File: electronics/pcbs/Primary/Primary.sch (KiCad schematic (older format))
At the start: 26 parts, among them J1 Line Sensor 1, J11 I2C Bus, J12 Battery, J13 Pololu_D24V50F5, J14 Magnet, J2 Line Sensor 2, J3 Line Sensor 3, J4 Line Sensor 4, J5 Line Sensor 5, J6 Line Sensor 6, J7 Servo, J8 Pololu_DRV8834, J9 Stepper Motor, P1 Digital, P10 CONN_01X01, P11 CONN_01X01, P12 CONN_01X01, P13 CONN_01X01, P2 Power, P3 Analog, P4 Analog, P5 PWM, P6 PWM, P7 Communication, P8 CONN_01X01, P9 CONN_01X01

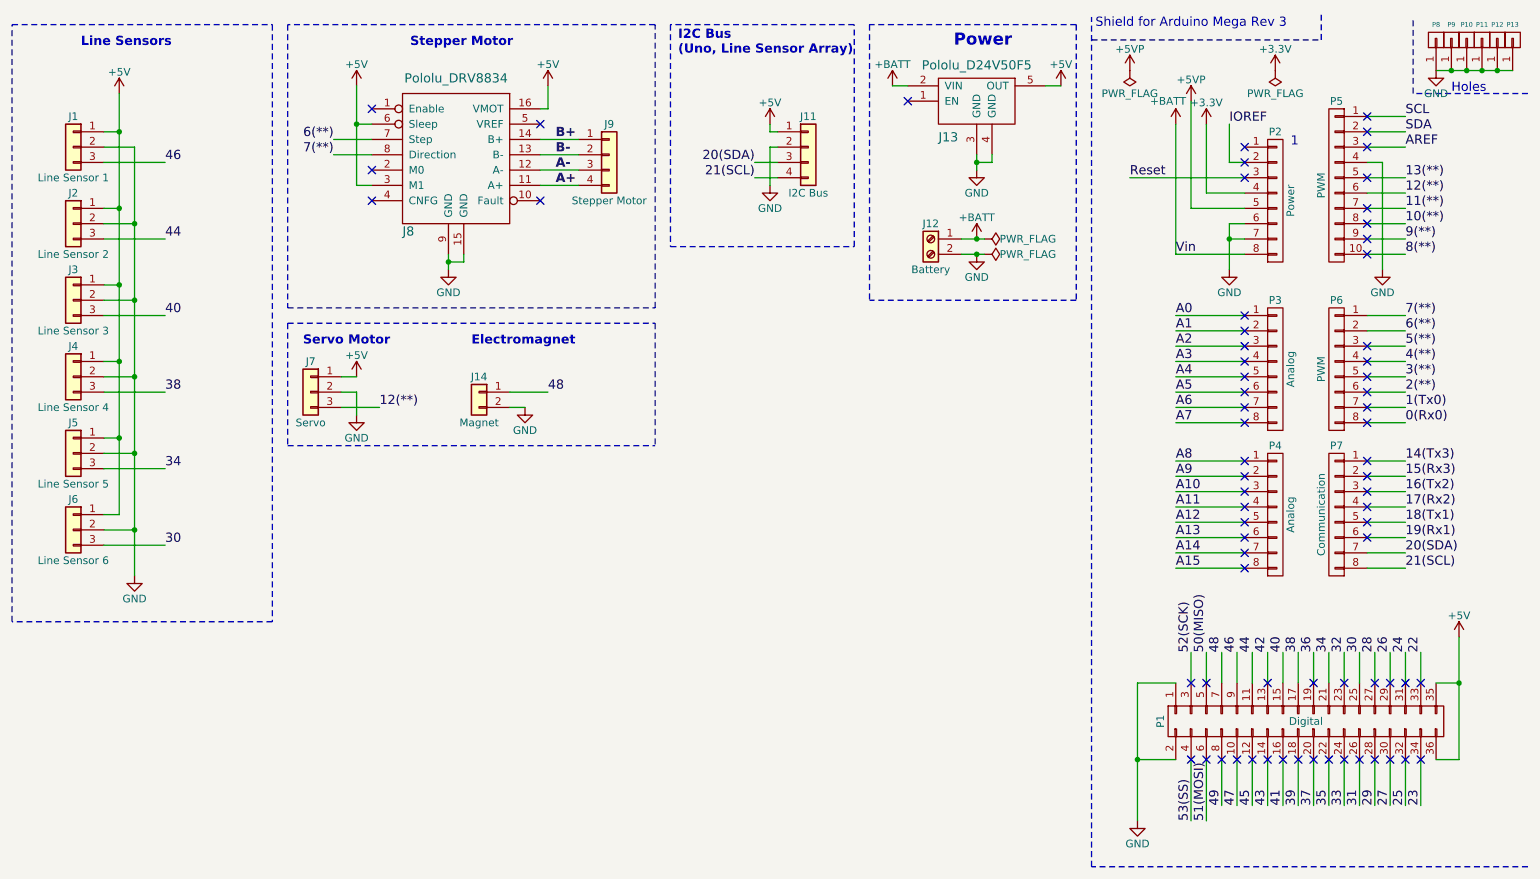
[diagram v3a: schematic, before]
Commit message: Primary PCB: Modified electromagnet circuit to power the magnet with a transistor.
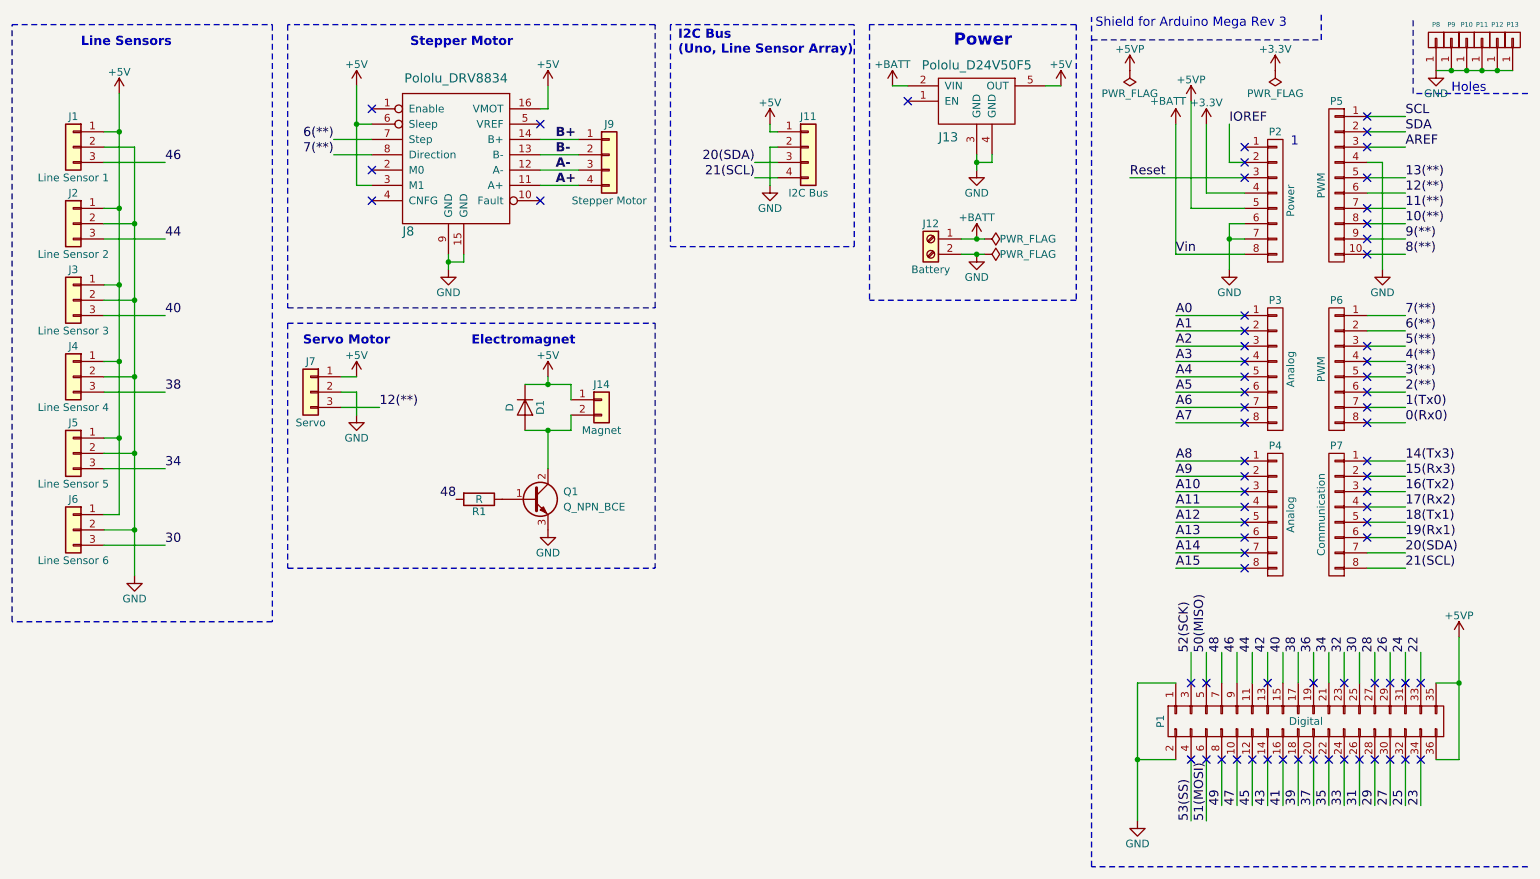
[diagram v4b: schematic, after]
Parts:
- added D1: D, Diodes_THT:D_DO-15_P5.08mm_Vertical_KathodeUp, symbol D
- added Q1: Q_NPN_BCE, TO_SOT_Packages_THT:TO-92_Inline_Wide, symbol Q_NPN_BCE
- added R1: R, Resistors_THT:R_Axial_DIN0309_L9.0mm_D3.2mm_P5.08mm_Vertical, symbol R
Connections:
- net +5V: now also J14.1 (Pin_1), D1.1 (K); no longer P1.35 (P35), P1.36 (P36)
- net +5VP: now also P1.35 (P35), P1.36 (P36)
- net 48: now also R1.2; no longer J14.1 (Pin_1)
- net GND: now also Q1.3 (E); no longer J14.2 (Pin_2)
- new net: D1.2 (A), J14.2 (Pin_2), Q1.2 (C)
- new net: Q1.1 (B), R1.1
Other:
- moved on the sheet: J14
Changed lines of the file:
@@
 Title "Primary Region V Bot"
 Date "2018-03-21"
-Rev "2"
+Rev "3"
 Comp "IEEE RAS (UT)"
-Comment1 "Rev 2: The Mega is now powered by +BATT"
-Comment2 ""
+Comment1 "Rev 3: The magnet is driven by a transistor now."
+Comment2 "Rev 2: The Mega is now powered by +BATT"
 Comment3 ""
 Comment4 ""
@@
 $EndComp
 $Comp
-L +5V #PWR05
-U 1 1 56D75AB8
-P 10750 4550
-F 0 "#PWR05" H 10750 4400 50  0001 C CNN
-F 1 "+5V" H 10750 4690 50  0000 C CNN
-F 2 "" H 10750 4550 50  0000 C CNN
-F 3 "" H 10750 4550 50  0000 C CNN
-	1    10750 4550
-	1    0    0    -1
-$EndComp
-$Comp
 L Conn_01x03 J3
 U 1 1 5AB06CE7
@@
 $EndComp
 $Comp
-L GND #PWR06
+L GND #PWR05
 U 1 1 5AB07E69
 P 2100 4150
-F 0 "#PWR06" H 2100 3900 50  0001 C CNN
+F 0 "#PWR05" H 2100 3900 50  0001 C CNN
 F 1 "GND" H 2100 4000 50  0000 C CNN
 F 2 "" H 2100 4150 50  0000 C CNN
@@
 NoConn ~ 3650 1700
 $Comp
-L GND #PWR07
+L GND #PWR06
 U 1 1 5AB0A94E
 P 4150 2150
-F 0 "#PWR07" H 4150 1900 50  0001 C CNN
+F 0 "#PWR06" H 4150 1900 50  0001 C CNN
 F 1 "GND" H 4150 2000 50  0000 C CNN
 F 2 "" H 4150 2150 50  0000 C CNN
@@
 Stepper Motor
 $Comp
-L +5V #PWR08
+L +5V #PWR07
 U 1 1 5AB0B79A
 P 2000 1000
-F 0 "#PWR08" H 2000 850 50  0001 C CNN
+F 0 "#PWR07" H 2000 850 50  0001 C CNN
 F 1 "+5V" H 2000 1140 50  0000 C CNN
 F 2 "" H 2000 1000 50  0000 C CNN
@@
 $EndComp
 $Comp
-L +5V #PWR09
+L +5V #PWR08
 U 1 1 5AB0BB75
 P 3550 950
-F 0 "#PWR09" H 3550 800 50  0001 C CNN
+F 0 "#PWR08" H 3550 800 50  0001 C CNN
 F 1 "+5V" H 3550 1090 50  0000 C CNN
 F 2 "" H 3550 950 50  0000 C CNN
@@
 $EndComp
 $Comp
-L +5V #PWR010
+L +5V #PWR09
 U 1 1 5AB0BCF7
 P 4800 950
-F 0 "#PWR010" H 4800 800 50  0001 C CNN
+F 0 "#PWR09" H 4800 800 50  0001 C CNN
 F 1 "+5V" H 4800 1090 50  0000 C CNN
 F 2 "" H 4800 950 50  0000 C CNN
@@
 $EndComp
 $Comp
-L +5V #PWR011
-U 1 1 5AB0C699
-P 6250 1200
-F 0 "#PWR011" H 6250 1050 50  0001 C CNN
-F 1 "+5V" H 6250 1340 50  0000 C CNN
-F 2 "" H 6250 1200 50  0000 C CNN
-F 3 "" H 6250 1200 50  0000 C CNN
-	1    6250 1200
-	1    0    0    -1
-$EndComp
-$Comp
-L GND #PWR012
+L GND #PWR010
 U 1 1 5AB0CA84
 P 6250 1600
-F 0 "#PWR012" H 6250 1350 50  0001 C CNN
+F 0 "#PWR010" H 6250 1350 50  0001 C CNN
 F 1 "GND" H 6250 1450 50  0000 C CNN
 F 2 "" H 6250 1600 50  0000 C CNN
@@
 Servo Motor
 $Comp
-L +5V #PWR013
+L +5V #PWR011
 U 1 1 5AB127F7
 P 3550 2850
-F 0 "#PWR013" H 3550 2700 50  0001 C CNN
+F 0 "#PWR011" H 3550 2700 50  0001 C CNN
 F 1 "+5V" H 3550 2990 50  0000 C CNN
 F 2 "" H 3550 2850 50  0000 C CNN
@@
 $EndComp
 $Comp
-L GND #PWR014
+L GND #PWR012
 U 1 1 5AB1284A
 P 3550 3100
-F 0 "#PWR014" H 3550 2850 50  0001 C CNN
+F 0 "#PWR012" H 3550 2850 50  0001 C CNN
 F 1 "GND" H 3550 2950 50  0000 C CNN
 F 2 "" H 3550 3100 50  0000 C CNN
@@
 	3550 2850 3450 2850
 Wire Notes Line
-	3100 2500 3100 3300
-Wire Notes Line
-	3100 3300 5500 3300
+	3100 2500 3100 4100
+Wire Notes Line
+	3100 4100 5500 4100
 Wire Notes Line
 	3100 2500 5500 2500
@@
 NoConn ~ 7150 1050
 $Comp
-L GND #PWR015
+L GND #PWR013
 U 1 1 5AB13861
 P 7600 1500
-F 0 "#PWR015" H 7600 1250 50  0001 C CNN
+F 0 "#PWR013" H 7600 1250 50  0001 C CNN
 F 1 "GND" H 7600 1350 50  0000 C CNN
 F 2 "" H 7600 1500 50  0000 C CNN
@@
 Connection ~ 7600 1450
 $Comp
-L +BATT #PWR016
+L +BATT #PWR014
 U 1 1 5AB13B80
 P 7050 950
-F 0 "#PWR016" H 7050 800 50  0001 C CNN
+F 0 "#PWR014" H 7050 800 50  0001 C CNN
 F 1 "+BATT" H 7050 1090 50  0000 C CNN
 F 2 "" H 7050 950 50  0001 C CNN
@@
 $EndComp
 $Comp
-L +BATT #PWR017
+L +BATT #PWR015
 U 1 1 5AB16019
 P 7600 1950
-F 0 "#PWR017" H 7600 1800 50  0001 C CNN
+F 0 "#PWR015" H 7600 1800 50  0001 C CNN
 F 1 "+BATT" H 7600 2090 50  0000 C CNN
 F 2 "" H 7600 1950 50  0001 C CNN
@@
 $EndComp
 $Comp
-L GND #PWR018
+L GND #PWR016
 U 1 1 5AB16072
 P 7600 2050
-F 0 "#PWR018" H 7600 1800 50  0001 C CNN
+F 0 "#PWR016" H 7600 1800 50  0001 C CNN
 F 1 "GND" H 7600 1900 50  0000 C CNN
 F 2 "" H 7600 2050 50  0000 C CNN
@@
 $EndComp
 $Comp
-L PWR_FLAG #FLG019
+L PWR_FLAG #FLG017
 U 1 1 5AB160ED
 P 7650 1950
-F 0 "#FLG019" H 7650 2025 50  0001 C CNN
+F 0 "#FLG017" H 7650 2025 50  0001 C CNN
 F 1 "PWR_FLAG" V 7650 2050 50  0000 L CNN
 F 2 "" H 7650 1950 50  0001 C CNN
@@
 $EndComp
 $Comp
-L PWR_FLAG #FLG020
+L PWR_FLAG #FLG018
 U 1 1 5AB1614D
 P 7650 2050
-F 0 "#FLG020" H 7650 2125 50  0001 C CNN
+F 0 "#FLG018" H 7650 2125 50  0001 C CNN
 F 1 "PWR_FLAG" V 7650 2150 50  0000 L CNN
 F 2 "" H 7650 2050 50  0001 C CNN
@@
 Connection ~ 7600 2050
 $Comp
-L PWR_FLAG #FLG021
+L PWR_FLAG #FLG019
 U 1 1 5AB1CAC7
 P 8600 850
-F 0 "#FLG021" H 8600 925 50  0001 C CNN
+F 0 "#FLG019" H 8600 925 50  0001 C CNN
 F 1 "PWR_FLAG" H 8600 1000 50  0000 C CNN
 F 2 "" H 8600 850 50  0001 C CNN
@@
 $EndComp
 $Comp
-L PWR_FLAG #FLG022
+L PWR_FLAG #FLG020
 U 1 1 5AB1CCDE
 P 9550 850
-F 0 "#FLG022" H 9550 925 50  0001 C CNN
+F 0 "#FLG020" H 9550 925 50  0001 C CNN
 F 1 "PWR_FLAG" H 9550 1000 50  0000 C CNN
 F 2 "" H 9550 850 50  0001 C CNN
@@
 $EndComp
 $Comp
-L +3.3V #PWR023
+L +3.3V #PWR021
 U 1 1 5AB1CD37
 P 9550 850
-F 0 "#PWR023" H 9550 700 50  0001 C CNN
+F 0 "#PWR021" H 9550 700 50  0001 C CNN
 F 1 "+3.3V" H 9550 990 50  0000 C CNN
 F 2 "" H 9550 850 50  0000 C CNN
@@
 L Conn_01x02 J14
 U 1 1 5AB1EC74
-P 4350 2950
-F 0 "J14" H 4350 3050 50  0000 C CNN
-F 1 "Magnet" H 4350 2750 50  0000 C CNN
-F 2 "Connectors_Samtec:SL-102-X-XX_1x02" H 4350 2950 50  0001 C CNN
-F 3 "" H 4350 2950 50  0001 C CNN
-	1    4350 2950
-	-1   0    0    -1
-$EndComp
-$Comp
-L GND #PWR024
+P 5150 3000
+F 0 "J14" H 5150 3100 50  0000 C CNN
+F 1 "Magnet" H 5150 2800 50  0000 C CNN
+F 2 "Connectors_Samtec:SL-102-X-XX_1x02" H 5150 3000 50  0001 C CNN
+F 3 "" H 5150 3000 50  0001 C CNN
+	1    5150 3000
+	1    0    0    -1
+$EndComp
+$Comp
+L GND #PWR022
 U 1 1 5AB1ECFA
-P 4650 3050
-F 0 "#PWR024" H 4650 2800 50  0001 C CNN
-F 1 "GND" H 4650 2900 50  0000 C CNN
-F 2 "" H 4650 3050 50  0000 C CNN
-F 3 "" H 4650 3050 50  0000 C CNN
-	1    4650 3050
-	1    0    0    -1
-$EndComp
-Wire Wire Line
-	4550 3050 4650 3050
+P 4800 3850
+F 0 "#PWR022" H 4800 3600 50  0001 C CNN
+F 1 "GND" H 4800 3700 50  0000 C CNN
+F 2 "" H 4800 3850 50  0000 C CNN
+F 3 "" H 4800 3850 50  0000 C CNN
+	1    4800 3850
+	1    0    0    -1
+$EndComp
 Text Notes 4300 2650 0    60   ~ 12
 Electromagnet
-Wire Wire Line
-	4550 2950 4800 2950
-Wire Notes Line
-	5500 2500 5500 3300
+Wire Notes Line
+	5500 2500 5500 4100
 Text Label 4850 1300 0    60   ~ 12
 B+
@@
 Text Label 3700 3050 0    60   ~ 0
 12(**)
-Text Label 4800 2950 0    60   ~ 0
+Text Label 4200 3650 2    60   ~ 0
 48
 Text Label 2300 1450 0    60   ~ 0
@@
 NoConn ~ 9500 4850
 $Comp
-L +5VP #PWR025
+L +5VP #PWR023
 U 1 1 5AB27247
 P 9000 1050
-F 0 "#PWR025" H 9000 900 50  0001 C CNN
+F 0 "#PWR023" H 9000 900 50  0001 C CNN
 F 1 "+5VP" H 9000 1190 50  0000 C CNN
 F 2 "" H 9000 1050 50  0001 C CNN
@@
 $EndComp
 $Comp
-L +5V #PWR026
+L +5V #PWR024
 U 1 1 5AB272C7
 P 8150 950
-F 0 "#PWR026" H 8150 800 50  0001 C CNN
+F 0 "#PWR024" H 8150 800 50  0001 C CNN
 F 1 "+5V" H 8150 1090 50  0000 C CNN
 F 2 "" H 8150 950 50  0000 C CNN
@@
 	8050 950  8150 950
 $Comp
-L +5VP #PWR027
+L +5VP #PWR025
 U 1 1 5AB2840B
 P 8600 850
-F 0 "#PWR027" H 8600 700 50  0001 C CNN
+F 0 "#PWR025" H 8600 700 50  0001 C CNN
 F 1 "+5VP" H 8600 990 50  0000 C CNN
 F 2 "" H 8600 850 50  0001 C CNN
@@
 $EndComp
 $Comp
-L GND #PWR028
+L GND #PWR026
 U 1 1 5AB165B1
 P 10600 850
-F 0 "#PWR028" H 10600 600 50  0001 C CNN
+F 0 "#PWR026" H 10600 600 50  0001 C CNN
 F 1 "GND" H 10600 700 50  0000 C CNN
 F 2 "" H 10600 850 50  0000 C CNN
@@
 Connection ~ 11000 850
 $Comp
-L +BATT #PWR029
+L +BATT #PWR027
 U 1 1 5AB2CF23
 P 8900 1200
-F 0 "#PWR029" H 8900 1050 50  0001 C CNN
+F 0 "#PWR027" H 8900 1050 50  0001 C CNN
 F 1 "+BATT" H 8850 1350 50  0000 C CNN
 F 2 "" H 8900 1200 50  0001 C CNN
@@
 Wire Wire Line
 	6300 1550 6150 1550
+$Comp
+L R R1
+U 1 1 5AC00307
+P 4350 3650
+F 0 "R1" V 4430 3650 50  0000 C CNN
+F 1 "R" V 4350 3650 50  0000 C CNN
+F 2 "Resistors_THT:R_Axial_DIN0309_L9.0mm_D3.2mm_P5.08mm_Vertical" V 4280 3650 50  0001 C CNN
+F 3 "" H 4350 3650 50  0001 C CNN
+	1    4350 3650
+	0    1    1    0
+$EndComp
+$Comp
+L Q_NPN_BCE Q1
+U 1 1 5AC00358
+P 4700 3650
+F 0 "Q1" H 4900 3700 50  0000 L CNN
+F 1 "Q_NPN_BCE" H 4900 3600 50  0000 L CNN
+F 2 "TO_SOT_Packages_THT:TO-92_Inline_Wide" H 4900 3750 50  0001 C CNN
+F 3 "" H 4700 3650 50  0001 C CNN
+	1    4700 3650
+	1    0    0    -1
+$EndComp
+$Comp
+L +5V #PWR028
+U 1 1 5AC005CD
+P 4800 2850
+F 0 "#PWR028" H 4800 2700 50  0001 C CNN
+F 1 "+5V" H 4800 2990 50  0000 C CNN
+F 2 "" H 4800 2850 50  0000 C CNN
+F 3 "" H 4800 2850 50  0000 C CNN
+	1    4800 2850
+	1    0    0    -1
+$EndComp
+$Comp
+L +5V #PWR029
+U 1 1 5AC026E1
+P 6250 1200
+F 0 "#PWR029" H 6250 1050 50  0001 C CNN
+F 1 "+5V" H 6250 1340 50  0000 C CNN
+F 2 "" H 6250 1200 50  0000 C CNN
+F 3 "" H 6250 1200 50  0000 C CNN
+	1    6250 1200
+	1    0    0    -1
+$EndComp
+$Comp
+L D D1
+U 1 1 5AC02CCD
+P 4650 3050
+F 0 "D1" H 4650 3150 50  0000 C CNN
+F 1 "D" H 4650 2950 50  0000 C CNN
+F 2 "Diodes_THT:D_DO-15_P5.08mm_Vertical_KathodeUp" H 4650 3050 50  0001 C CNN
+F 3 "" H 4650 3050 50  0001 C CNN
+	1    4650 3050
+	0    1    1    0
+$EndComp
+Wire Wire Line
+	4950 2900 4950 3000
+Wire Wire Line
+	4650 2900 4950 2900
+Wire Wire Line
+	4800 2900 4800 2850
+Connection ~ 4800 2900
+Wire Wire Line
+	4650 3200 4950 3200
+Wire Wire Line
+	4800 3200 4800 3450
+Wire Wire Line
+	4950 3200 4950 3100
+Connection ~ 4800 3200
+$Comp
+L +5VP #PWR030
+U 1 1 5AC03CD4
+P 10750 4550
+F 0 "#PWR030" H 10750 4400 50  0001 C CNN
+F 1 "+5VP" H 10750 4690 50  0000 C CNN
+F 2 "" H 10750 4550 50  0001 C CNN
+F 3 "" H 10750 4550 50  0001 C CNN
+	1    10750 4550
+	1    0    0    -1
+$EndComp
 $EndSCHEMATC

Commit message: Primary PCB: Corrected transistor pinout and footprint. Gave a value to the resistor attached to the transistor.
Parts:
- D1: value D -> 1N914
- Q1: footprint TO_SOT_Packages_THT:TO-92_Inline_Wide -> TO_SOT_Packages_THT:TO-18-3; symbol Q_NPN_BCE -> Q_NPN_EBC
- R1: value R -> 220
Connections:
- net GND: now also Q1.1 (E); no longer Q1.3 (E)
- net at D1.2 (A), J14.2 (Pin_2): now also Q1.3 (C); no longer Q1.2 (C)
- net at R1.1: now also Q1.2 (B); no longer Q1.1 (B)
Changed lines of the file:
@@
 P 4350 3650
 F 0 "R1" V 4430 3650 50  0000 C CNN
-F 1 "R" V 4350 3650 50  0000 C CNN
+F 1 "220" V 4350 3650 50  0000 C CNN
 F 2 "Resistors_THT:R_Axial_DIN0309_L9.0mm_D3.2mm_P5.08mm_Vertical" V 4280 3650 50  0001 C CNN
 F 3 "" H 4350 3650 50  0001 C CNN
@@
 $EndComp
 $Comp
-L Q_NPN_BCE Q1
+L Q_NPN_EBC Q1
 U 1 1 5AC00358
 P 4700 3650
 F 0 "Q1" H 4900 3700 50  0000 L CNN
 F 1 "Q_NPN_BCE" H 4900 3600 50  0000 L CNN
-F 2 "TO_SOT_Packages_THT:TO-92_Inline_Wide" H 4900 3750 50  0001 C CNN
+F 2 "TO_SOT_Packages_THT:TO-18-3" H 4900 3750 50  0001 C CNN
 F 3 "" H 4700 3650 50  0001 C CNN
 	1    4700 3650
@@
 P 4650 3050
 F 0 "D1" H 4650 3150 50  0000 C CNN
-F 1 "D" H 4650 2950 50  0000 C CNN
+F 1 "1N914" H 4650 2950 50  0000 C CNN
 F 2 "Diodes_THT:D_DO-15_P5.08mm_Vertical_KathodeUp" H 4650 3050 50  0001 C CNN
 F 3 "" H 4650 3050 50  0001 C CNN

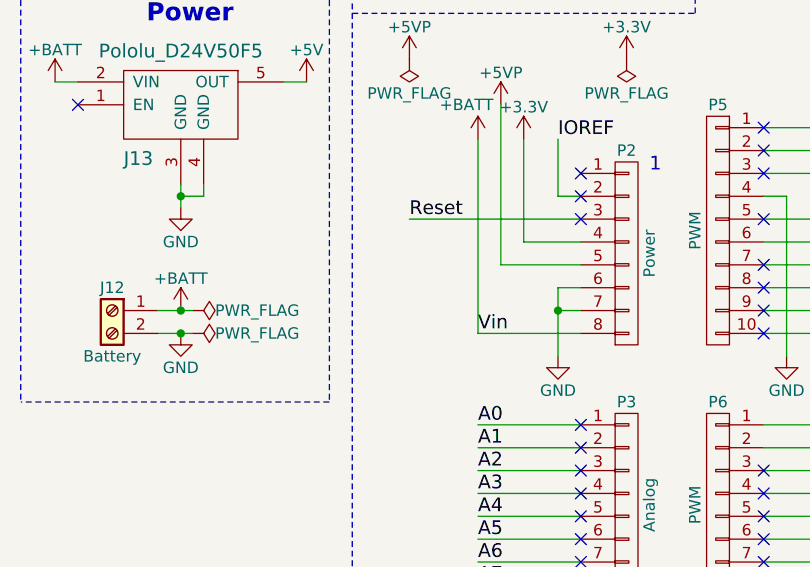
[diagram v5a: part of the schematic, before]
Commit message: Primary PCB: Added Reset button.
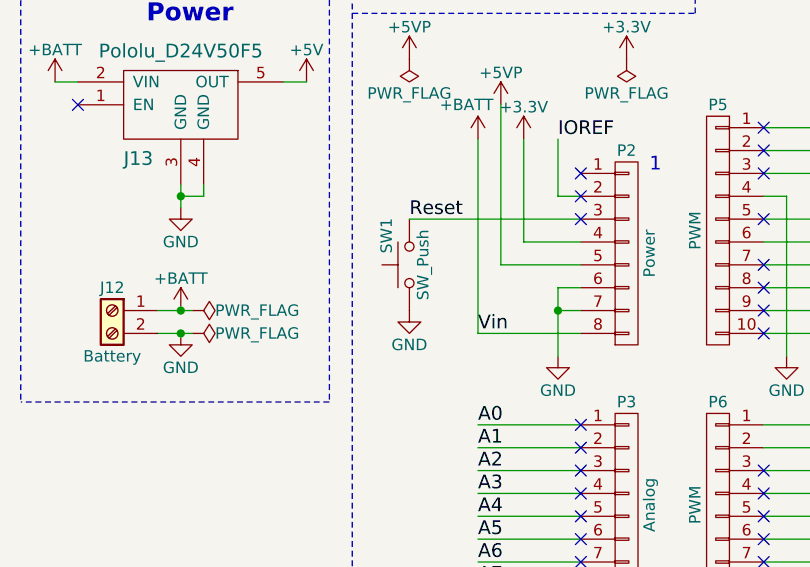
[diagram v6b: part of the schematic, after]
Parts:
- added SW1: SW_Push, Buttons_Switches_THT:SW_PUSH_6mm_h4.3mm, symbol SW_Push
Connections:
- net GND: now also SW1.1
- net Reset: now also SW1.2
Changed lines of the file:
@@
 LIBS:contrib
 LIBS:valves
+LIBS:switches
 LIBS:Primary-cache
 EELAYER 25 0
@@
 	1    0    0    -1
 $EndComp
+$Comp
+L SW_Push SW1
+U 1 1 5AC1986B
+P 8600 1750
+F 0 "SW1" H 8650 1850 50  0000 L CNN
+F 1 "SW_Push" H 8600 1690 50  0000 C CNN
+F 2 "Buttons_Switches_THT:SW_PUSH_6mm_h4.3mm" H 8600 1950 50  0001 C CNN
+F 3 "" H 8600 1950 50  0001 C CNN
+	1    8600 1750
+	0    -1   -1   0
+$EndComp
+$Comp
+L GND #PWR031
+U 1 1 5AC199A6
+P 8600 1950
+F 0 "#PWR031" H 8600 1700 50  0001 C CNN
+F 1 "GND" H 8600 1800 50  0000 C CNN
+F 2 "" H 8600 1950 50  0000 C CNN
+F 3 "" H 8600 1950 50  0000 C CNN
+	1    8600 1950
+	1    0    0    -1
+$EndComp
